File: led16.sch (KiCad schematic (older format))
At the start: 32 parts

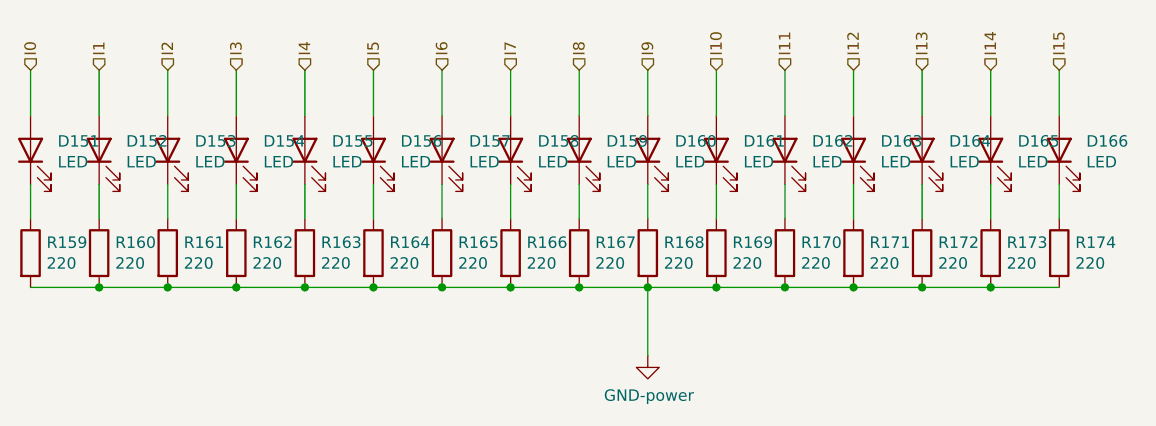
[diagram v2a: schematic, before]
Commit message: Added NAND GATES in ALU
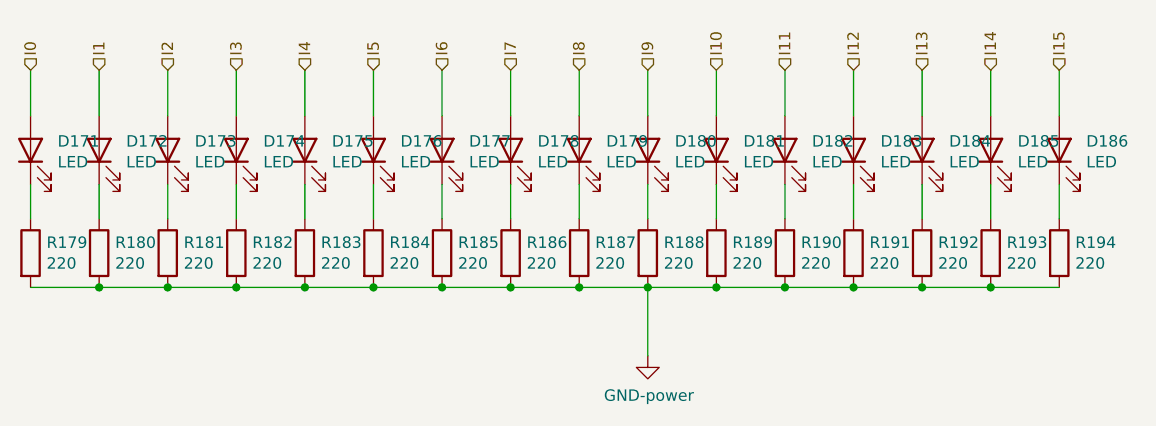
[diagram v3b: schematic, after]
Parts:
- renumbered D151 to D155, D152 to D156, D153 to D157, D154 to D158, D155 to D159, D156 to D160, D157 to D161, D158 to D162, D159 to D163, D160 to D164, D161 to D165, D162 to D166, D163 to D167, D164 to D168, D165 to D169, D166 to D170, R159 to R162, R160 to R163, R161 to R164, R162 to R165, R163 to R166, R164 to R167, R165 to R168, R166 to R169, R167 to R170, R168 to R171, R169 to R172, R170 to R173, R171 to R174, R172 to R175, R173 to R176, R174 to R177

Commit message: added 3-8 decoders to cu
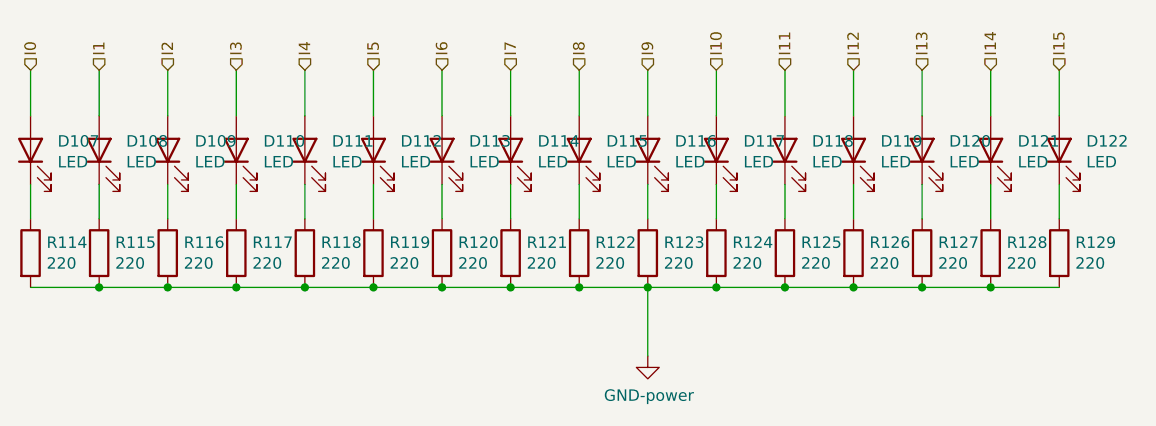
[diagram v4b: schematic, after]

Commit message: using new RAM and ROM,15bits baby
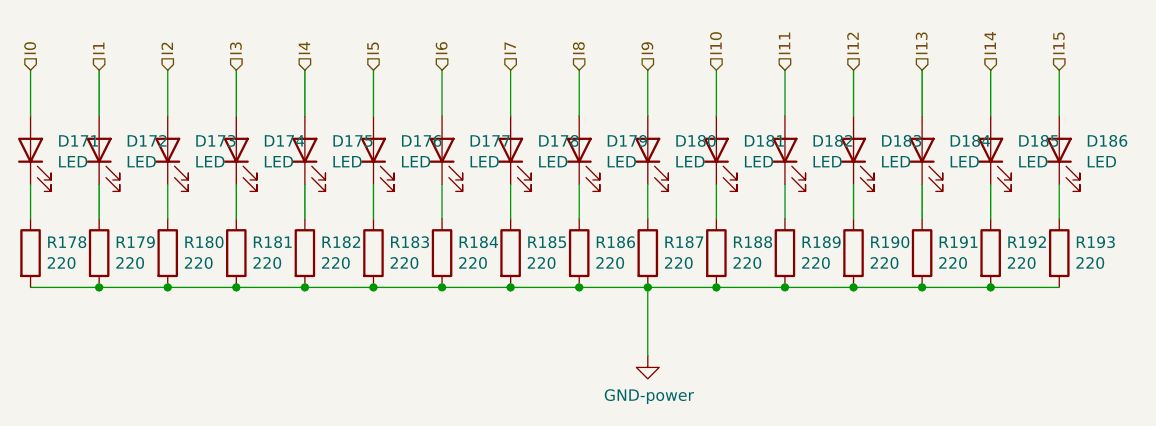
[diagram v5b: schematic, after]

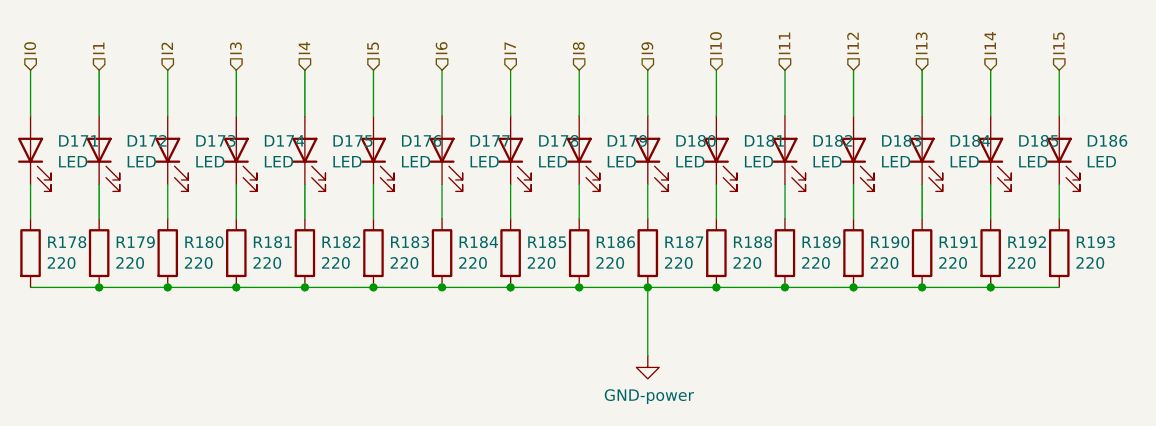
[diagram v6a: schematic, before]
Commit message: added power caps
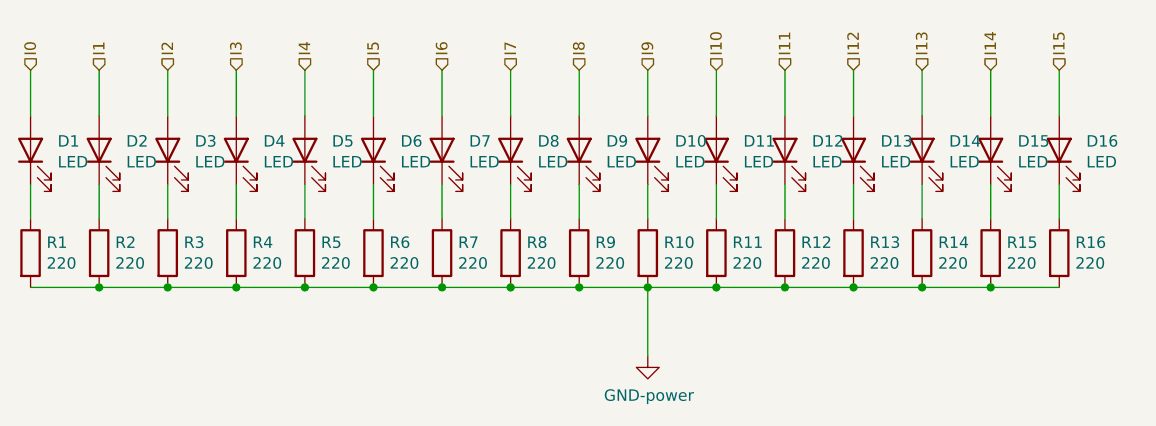
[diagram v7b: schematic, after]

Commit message: Added power connector
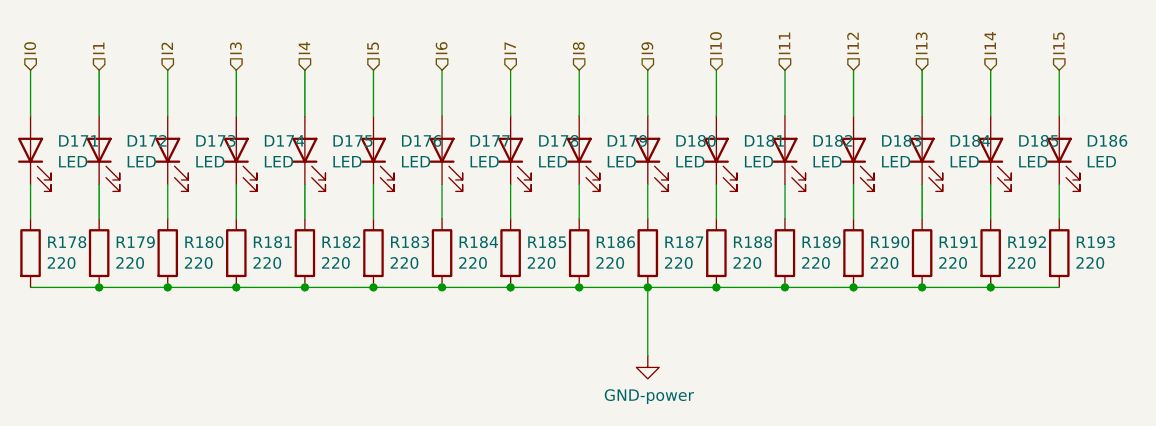
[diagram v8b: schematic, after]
